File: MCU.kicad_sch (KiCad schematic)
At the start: 20 parts, among them J10 UNCONNECTED_PB_PINS, J11 UNCONNECTED_PC_PINS, J8 UNCONNECTED_PA_PINS, Y1 ECS-2520MVLC-160-CN-TR

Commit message: aantal componenten veranderd.
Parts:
- removed R14: 47, Resistor_SMD:R_0805_2012Metric_Pad1.20x1.40mm_HandSolder, symbol Device:R
- removed Y1: ECS-2520MVLC-160-CN-TR, SamacSys_Parts:ECS2520MVLC160CNTR, symbol SamacSys_Parts:ECS-2520MVLC-160-CN-TR
- added C17, C18: 26p, Capacitor_SMD:C_0805_2012Metric_Pad1.18x1.45mm_HandSolder, symbol Device:C
- added Y1: ABM3-8.000MHZ-D2Y-T, Components:ABM3, symbol CustomSymbols:ABM3-8.000MHZ-D2Y-T
- J10: footprint Connector_PinHeader_2.54mm:PinHeader_1x13_P2.54mm_Vertical -> Connector_PinHeader_1.00mm:PinHeader_1x13_P1.00mm_Vertical
- J11: footprint Connector_PinHeader_2.54mm:PinHeader_1x14_P2.54mm_Vertical -> Connector_PinHeader_1.00mm:PinHeader_1x14_P1.00mm_Vertical
- J8: footprint Connector_PinHeader_2.54mm:PinHeader_1x07_P2.54mm_Vertical -> Connector_PinHeader_1.00mm:PinHeader_1x07_P1.00mm_Vertical
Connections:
- net GND: now also C17.2, C18.2
- net HSE_IN: now also C17.1, Y1.1
- net HSE_OUT: now also C18.1, Y1.2
- no-connect marks 4 -> 3

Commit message: beginsel aan pcb gemaakt
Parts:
- removed C?: 4.7u, Capacitor_SMD:C_0805_2012Metric_Pad1.18x1.45mm_HandSolder, symbol Device:C
- removed J10: UNCONNECTED_PB_PINS, Connector_PinHeader_1.00mm:PinHeader_1x13_P1.00mm_Vertical, symbol Connector:Conn_01x13_Pin
- removed J?: PROGRAM_PINS, Connector_PinHeader_2.54mm:PinHeader_2x05_P2.54mm_Vertical, symbol Connector_Generic:Conn_02x05_Counter_Clockwise
- added C?: 4.7u, Capacitor_SMD:C_0805_2012Metric_Pad1.18x1.45mm_HandSolder, symbol Device:C
- added C?: 100n, Capacitor_SMD:C_0805_2012Metric_Pad1.18x1.45mm_HandSolder, symbol Device:C
- added J10: TIM3_OUT_CONN, Connector_PinHeader_2.54mm:PinHeader_1x04_P2.54mm_Vertical, symbol Connector:Conn_01x04_Pin
- added J12: Conn_01x04_Pin, Connector_PinHeader_2.54mm:PinHeader_1x04_P2.54mm_Vertical, symbol Connector:Conn_01x04_Pin
- added J14: UNCONNECTED_Pb_PINS, Connector_PinHeader_1.00mm:PinHeader_1x11_P1.00mm_Vertical, symbol Connector:Conn_01x11_Pin
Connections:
- net +3V0: now also C?.1
- net GND: now also C?.2, C?.2, J12.4 (Pin_4)
- net IR_SIG2: now also U?.28 (PB2); no longer U?.26 (PB0)
- net IR_SIG3: now also U?.55 (PB3); no longer U?.27 (PB1)
- net NRST: now also J12.3 (Pin_3)
- net PB10: now also J14.7 (Pin_7)
- net PB12: now also J14.8 (Pin_8)
- net PB13: now also J14.9 (Pin_9)
- net PB14: now also J14.10 (Pin_10)
- net PB15: now also J14.11 (Pin_11)
- net PB2: now also J14.1 (Pin_1); no longer U?.28 (PB2)
- net PB3: now also J14.2 (Pin_2); no longer U?.55 (PB3)
- net PB4: now also J10.3 (Pin_3)
- net PB5: now also J10.4 (Pin_4)
- net PB6: now also J14.3 (Pin_3)
- net PB7: now also J14.4 (Pin_4)
- net PB8: now also J14.5 (Pin_5)
- net PB9: now also J14.6 (Pin_6)
- net SDCLK: now also J12.2 (Pin_2)
- net SWDIO: now also J12.1 (Pin_1)
- net at U?.30 (VCAP1): now also C?.1
- new net PB0: J10.1 (Pin_1), U?.26 (PB0)
- new net PB1: J10.2 (Pin_2), U?.27 (PB1)
- no-connect marks 3 -> 0

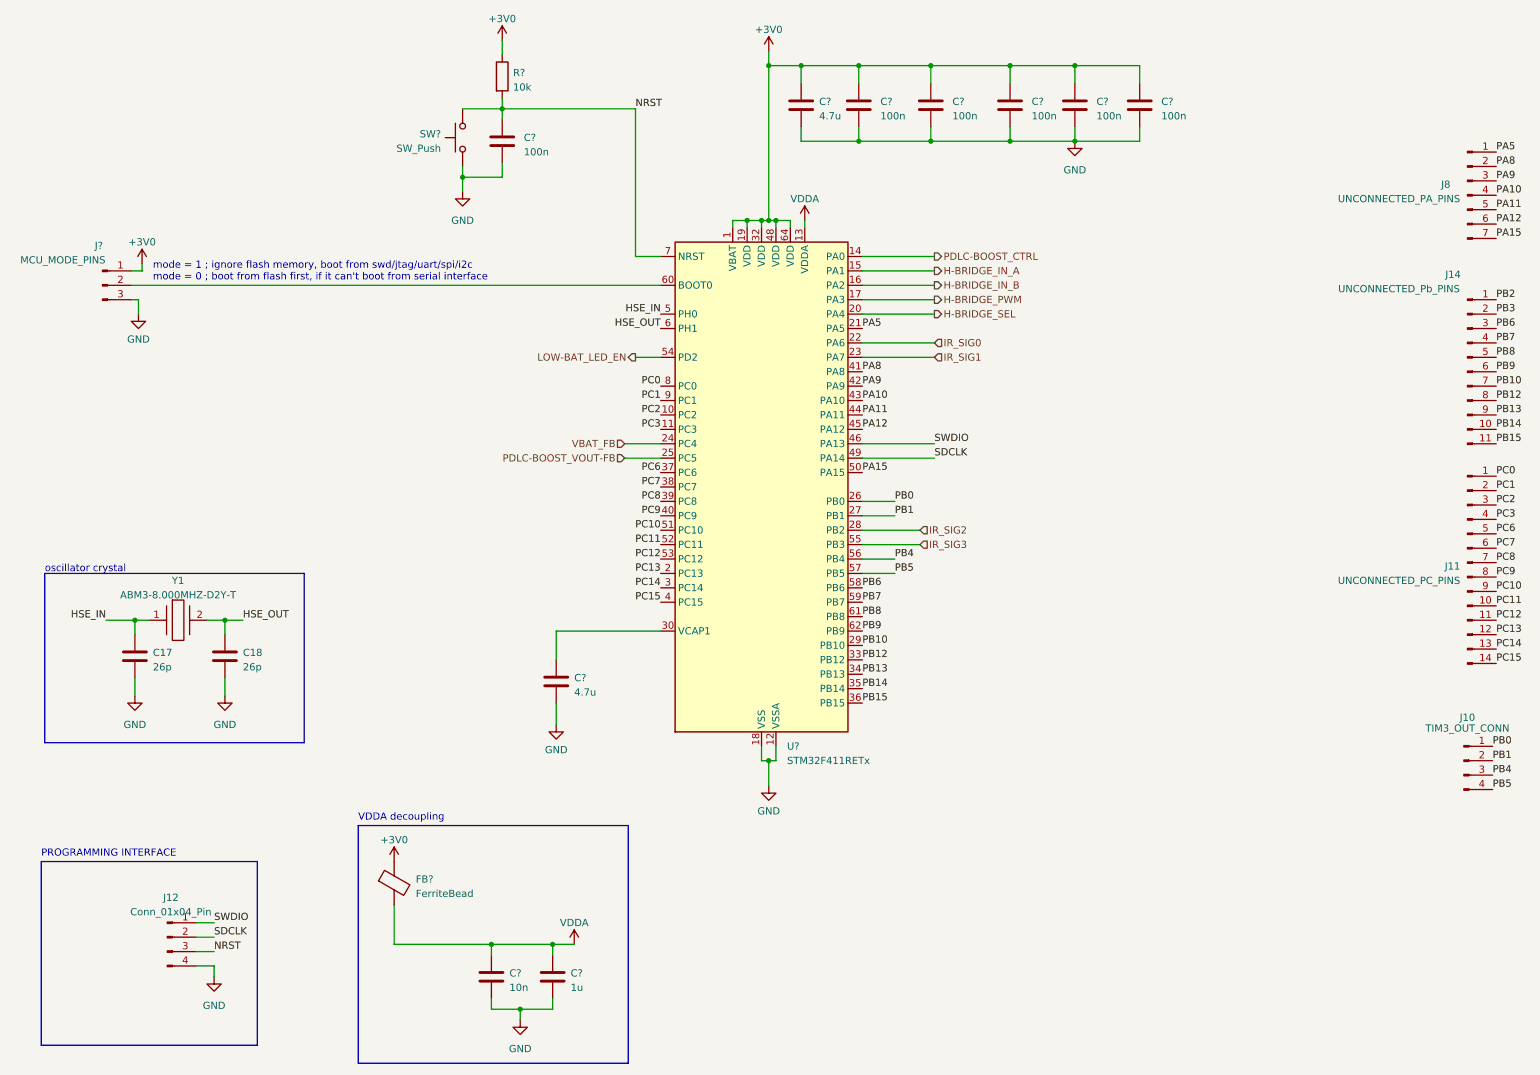
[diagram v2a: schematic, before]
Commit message: Alle verbindingen gelegt van de componenten.
Moet nog bij nog tekst bij de connectoren zetten. Ook zijn de unconnected pinnen weggehaald, omdat het onmogelijk maakt voor een 2 laags PCB.
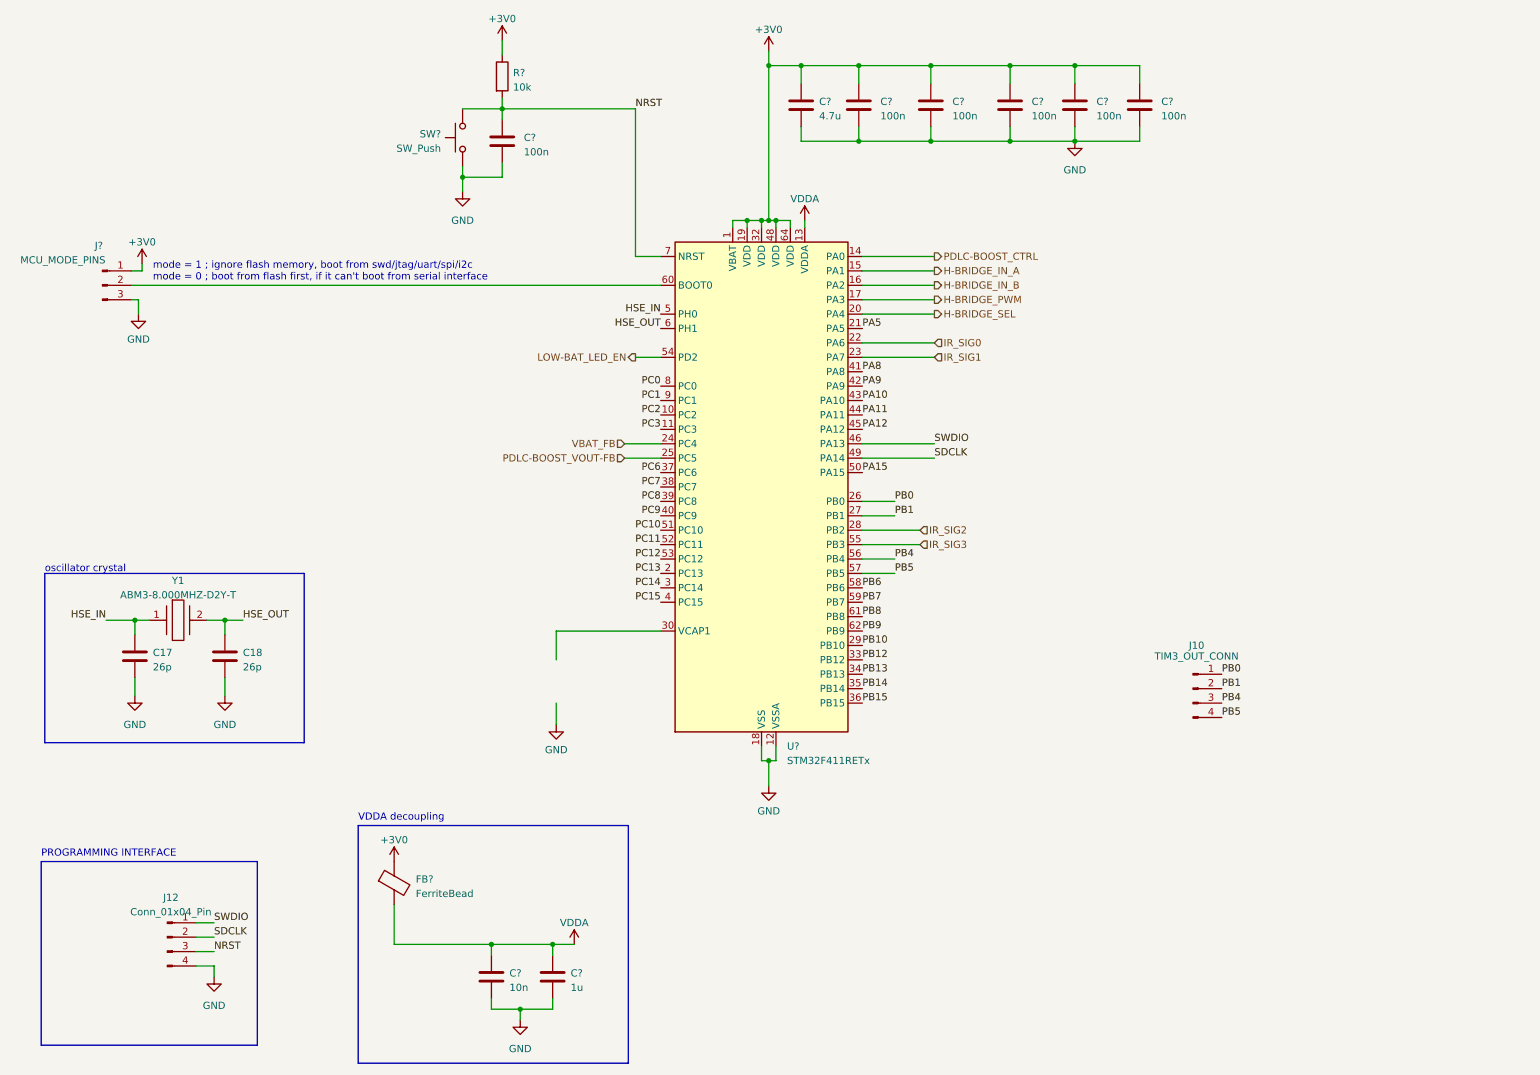
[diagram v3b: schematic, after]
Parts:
- removed C?: 4.7u, Capacitor_SMD:C_0805_2012Metric_Pad1.18x1.45mm_HandSolder, symbol Device:C
- removed J11: UNCONNECTED_PC_PINS, Connector_PinHeader_1.00mm:PinHeader_1x14_P1.00mm_Vertical, symbol Connector:Conn_01x14_Pin
- removed J14: UNCONNECTED_Pb_PINS, Connector_PinHeader_1.00mm:PinHeader_1x11_P1.00mm_Vertical, symbol Connector:Conn_01x11_Pin
- removed J8: UNCONNECTED_PA_PINS, Connector_PinHeader_1.00mm:PinHeader_1x07_P1.00mm_Vertical, symbol Connector:Conn_01x07_Pin
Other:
- moved on the sheet: J10

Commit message: nieuwe layout
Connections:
- net H-BRIDGE_IN_A: now also U?.16 (PA2); no longer U?.15 (PA1)
- net H-BRIDGE_IN_B: now also U?.15 (PA1); no longer U?.16 (PA2)
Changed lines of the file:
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@@
     (stroke (width 0) (type default))
   )
-  (wire (pts (xy 161.925 60.96) (xy 174.625 60.96))
+  (wire (pts (xy 161.925 60.96) (xy 174.752 60.96))
     (stroke (width 0) (type default))
   )
@@
     (stroke (width 0) (type default))
   )
-  (wire (pts (xy 161.925 58.42) (xy 174.625 58.42))
-    (stroke (width 0) (type default))
-  )
   (wire (pts (xy 91.44 40.005) (xy 91.44 41.91))
     (stroke (width 0) (type default))
@@
   )
   (wire (pts (xy 161.925 101.6) (xy 167.64 101.6))
+    (stroke (width 0) (type default))
+  )
+  (wire (pts (xy 161.925 58.42) (xy 174.752 58.42))
     (stroke (width 0) (type default))
   )
@@
     (effects (font (size 1.27 1.27)) (justify right))
   )
-  (hierarchical_label "H-BRIDGE_IN_A" (shape output) (at 174.625 58.42 0) (fields_autoplaced)
+  (hierarchical_label "H-BRIDGE_IN_A" (shape output) (at 174.752 60.96 0) (fields_autoplaced)
     (effects (font (size 1.27 1.27)) (justify left))
   )
@@
     (effects (font (size 1.27 1.27)) (justify right))
   )
-  (hierarchical_label "H-BRIDGE_IN_B" (shape output) (at 174.625 60.96 0) (fields_autoplaced)
-    (effects (font (size 1.27 1.27)) (justify left))
-  )
+  (hierarchical_label "H-BRIDGE_IN_B" (shape output) (at 174.752 58.42 0) (fields_autoplaced)
+    (effects (font (size 1.27 1.27)) (justify left))
+  )

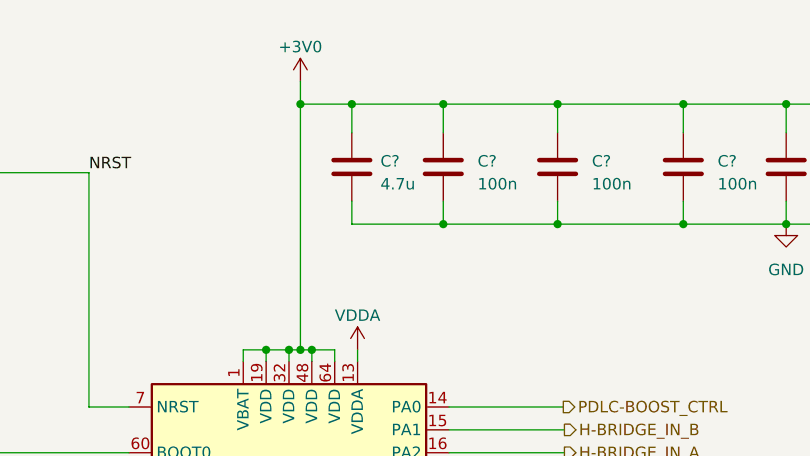
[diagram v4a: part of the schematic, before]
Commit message: Kleine veranderingen gebaseerd op feedback whatsapp
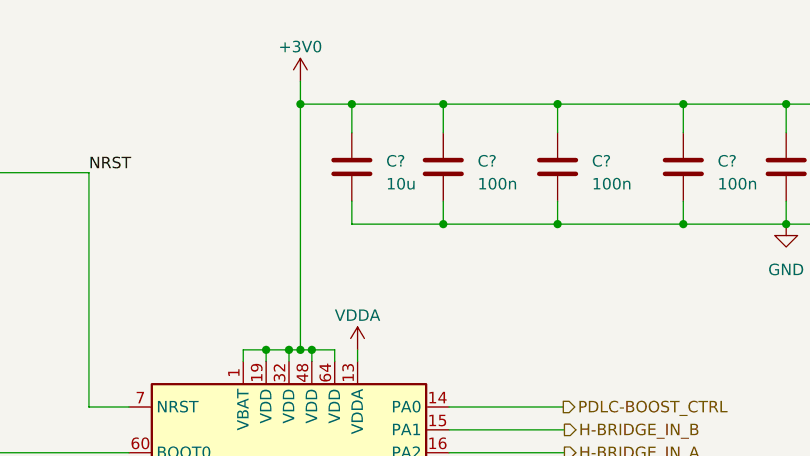
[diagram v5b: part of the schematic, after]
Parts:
- C?: value 4.7u -> 10u
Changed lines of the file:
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@@
   (symbol (lib_id "Device:C") (at 151.13 29.21 0) (unit 1)
     (in_bom yes) (on_board yes) (dnp no) (fields_autoplaced)
-    (property "Reference" "C?" (at 154.305 28.575 0)
+    (property "Reference" "C?" (at 154.94 28.575 0)
       (effects (font (size 1.27 1.27)) (justify left))
     )
-    (property "Value" "4.7u" (at 154.305 31.115 0)
+    (property "Value" "10u" (at 154.94 31.115 0)
       (effects (font (size 1.27 1.27)) (justify left))
     )

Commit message: updated schematic en interactive bom in de git
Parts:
- J?: footprint Connector_PinSocket_2.54mm:PinSocket_1x03_P2.54mm_Vertical -> Connector_PinHeader_2.54mm:PinHeader_1x03_P2.54mm_Vertical
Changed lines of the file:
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@@
       (effects (font (size 1.27 1.27)))
     )
-    (property "Footprint" "Connector_PinSocket_2.54mm:PinSocket_1x03_P2.54mm_Vertical" (at 27.94 60.96 0)
+    (property "Footprint" "Connector_PinHeader_2.54mm:PinHeader_1x03_P2.54mm_Vertical" (at 27.94 60.96 0)
       (effects (font (size 1.27 1.27)) hide)
     )

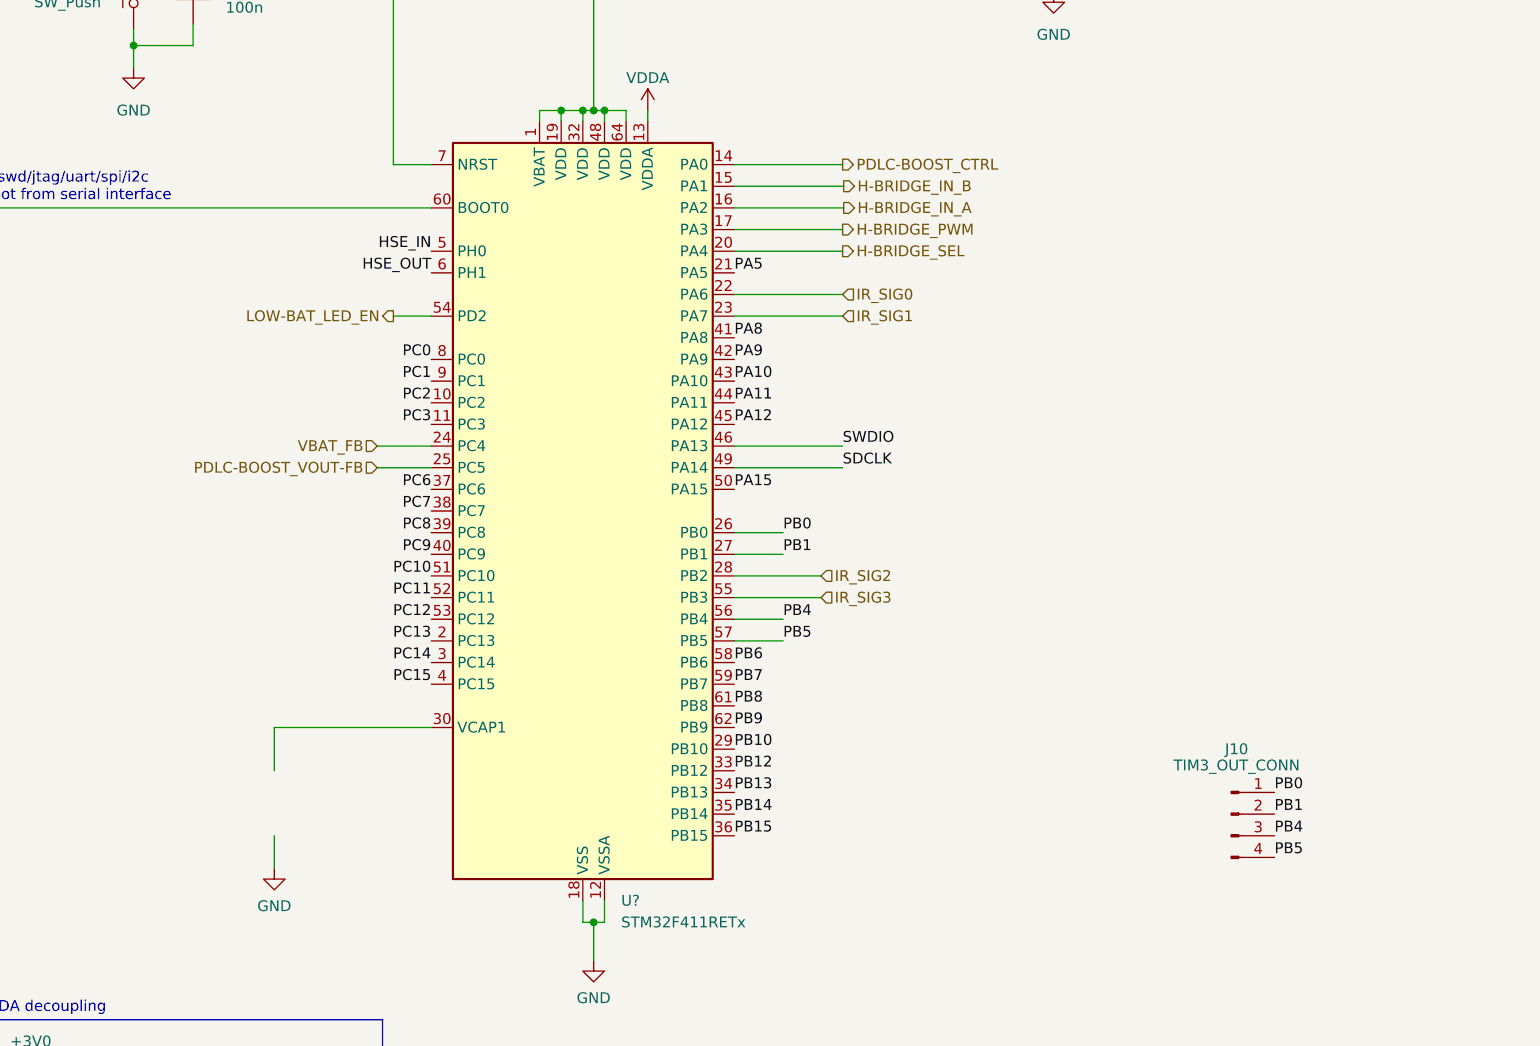
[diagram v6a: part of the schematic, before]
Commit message: PCBv2.01
Eerste versie van de tweede versie van de pcb prototype.
Nieuwe PDLC voeding, extra pinnen beschikbaar voor GUI inclusief voeding pinnen.
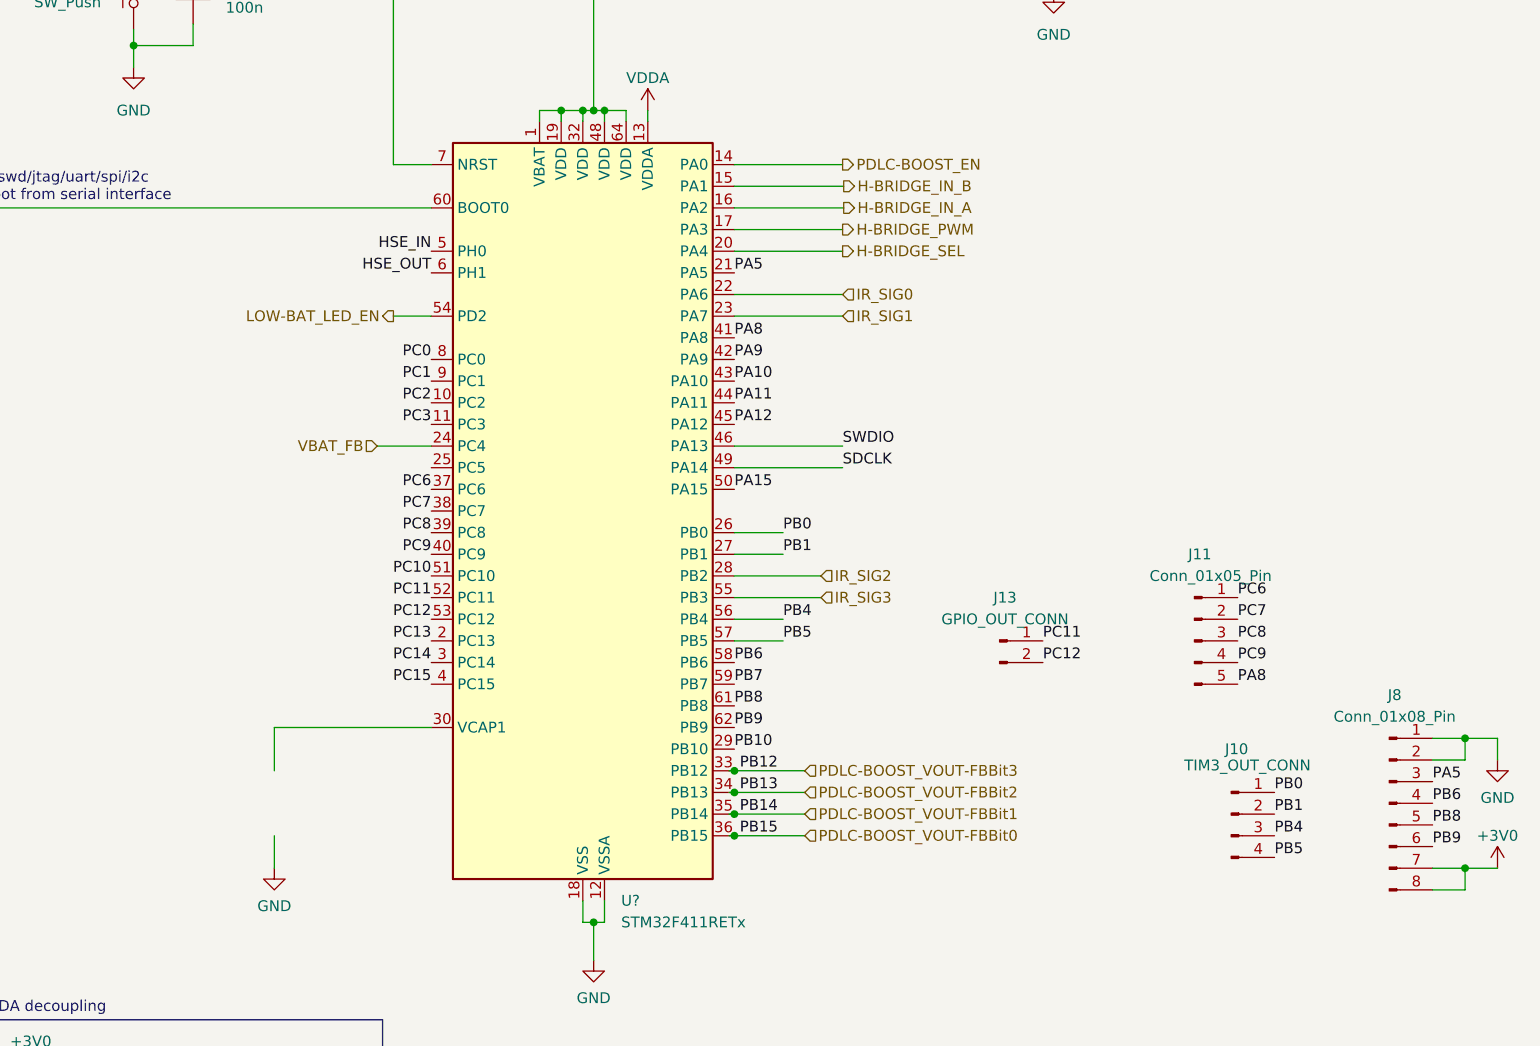
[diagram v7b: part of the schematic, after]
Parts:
- added J11: Conn_01x05_Pin, Connector_PinHeader_2.54mm:PinHeader_1x05_P2.54mm_Vertical, symbol Connector:Conn_01x05_Pin
- added J13: GPIO_OUT_CONN, Connector_PinHeader_2.54mm:PinHeader_1x02_P2.54mm_Vertical, symbol Connector:Conn_01x02_Pin
- added J8: Conn_01x08_Pin, Connector_PinHeader_2.54mm:PinHeader_1x08_P2.54mm_Vertical, symbol Connector:Conn_01x08_Pin
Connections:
- net +3V0: now also J8.7 (Pin_7), J8.8 (Pin_8)
- net GND: now also J8.1 (Pin_1), J8.2 (Pin_2)
- net PA5: now also J8.3 (Pin_3)
- net PA8: now also J11.5 (Pin_5)
- net PB6: now also J8.4 (Pin_4)
- net PB8: now also J8.5 (Pin_5)
- net PB9: now also J8.6 (Pin_6)
- net PC11: now also J13.1 (Pin_1)
- net PC12: now also J13.2 (Pin_2)
- net PC6: now also J11.1 (Pin_1)
- net PC7: now also J11.2 (Pin_2)
- net PC8: now also J11.3 (Pin_3)
- net PC9: now also J11.4 (Pin_4)
- net PB12 renamed PDLC-BOOST_VOUT-FBBit3
- net PB13 renamed PDLC-BOOST_VOUT-FBBit2
- net PB14 renamed PDLC-BOOST_VOUT-FBBit1
- net PB15 renamed PDLC-BOOST_VOUT-FBBit0
- net PDLC-BOOST_CTRL renamed PDLC-BOOST_EN
- net PDLC-BOOST_VOUT-FB: no longer names the net of U?.25 (PC5)
